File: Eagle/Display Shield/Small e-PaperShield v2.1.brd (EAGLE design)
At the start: 101.8 x 54.7 mm, 114 parts, among them J2 3300060P1-ST-TF-003A, J3 2.54-8p-male-SMD, J4 2.54-8p-male-SMD, J5 2.54-6p-male-SMD, J6 2.54-6p-male-SMD, J7 2.54-2x3p-female-SMD, Q10 MOSFET-P-044021001, Q11 2N7002, Q2 2N7002, Q3 MOSFET-P-044021001, Q5 MOSFET-P-044021001, Q7 MOSFET-P-044021001, Q8 2N7002, Q9 2N7002, SW1 BUTTON-4P-REINFORCE'TS-1188E', U2 XC6206-3.3-1300260P1, U3 74VHC125PW, U4 74VHC125PW, U5 GT20L16P1Y, U9 S-8120CNB-DRB-TF-G//200021001, X1 FH12-40S-0.5SH

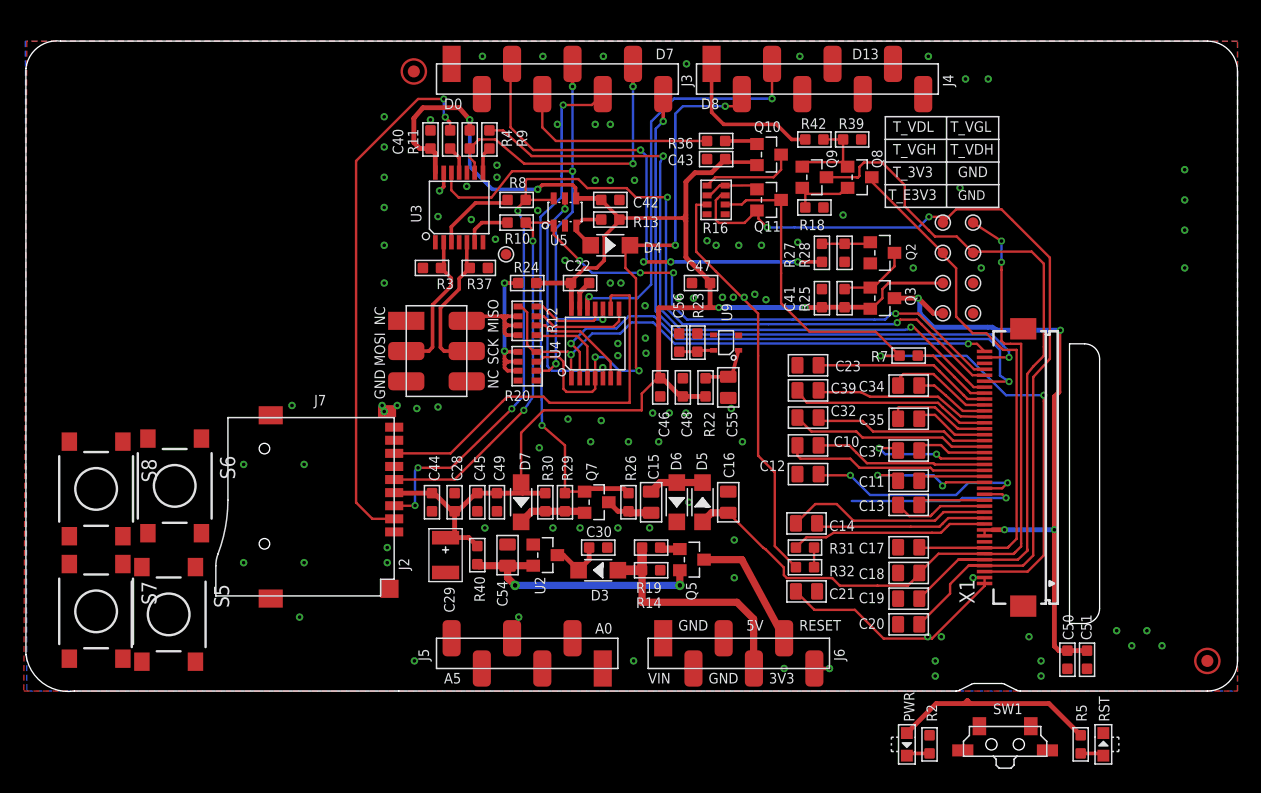
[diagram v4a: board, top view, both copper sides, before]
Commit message: DRC corrections for display shield
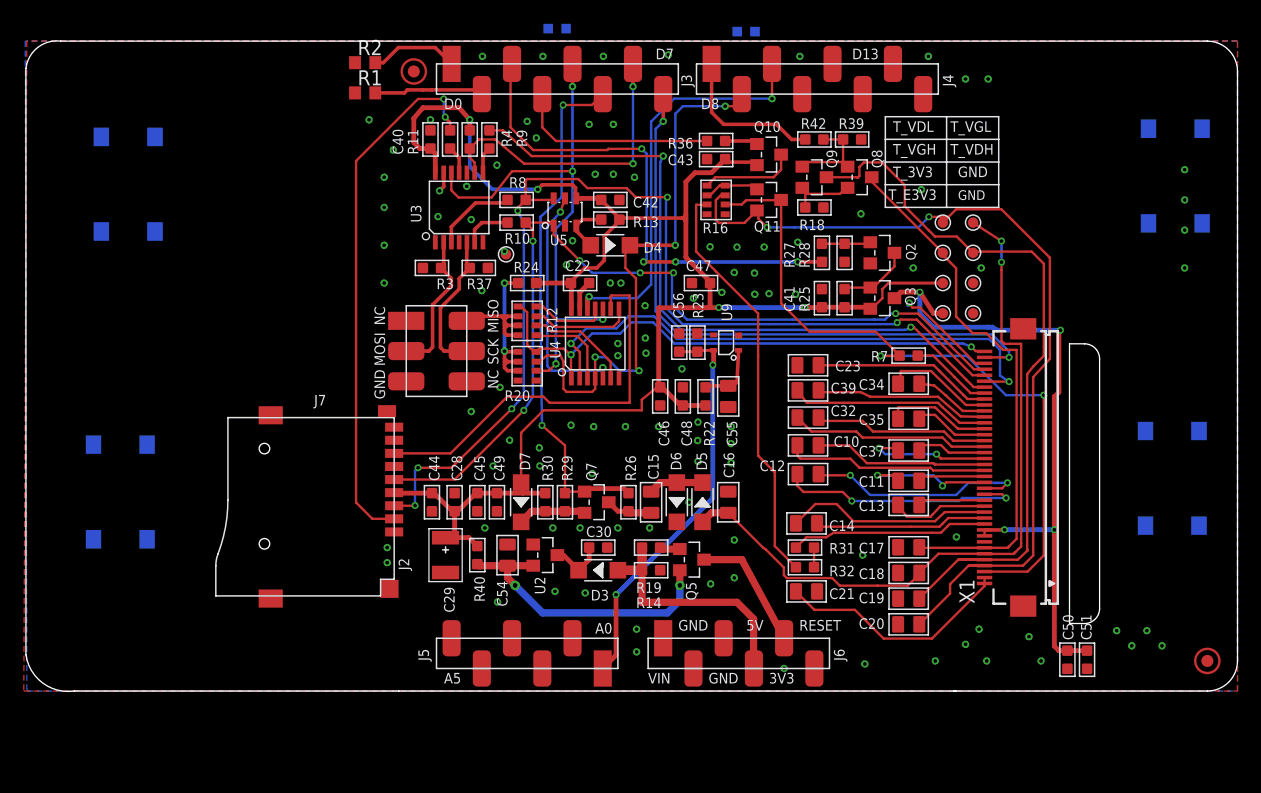
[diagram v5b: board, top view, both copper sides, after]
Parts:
- removed PWR: led-green, Discrete:LED-SIDE-VIEW-0603-RIGHT
- removed R5: 1k, Discrete:R0603
- removed RST: led-red, Discrete:LED-SIDE-VIEW-0603-RIGHT
- removed SW1: BUTTON-4P-REINFORCE'TS-1188E', Discrete:4P-SMD-7X3.5X3.5H
- added LED0: LED0, adafruit:CHIPLED_0603
- added LED1: LED1, adafruit:CHIPLED_0603
- added R1: 1k, rcl:R0603
- R2: device Discrete:R0603 -> rcl:R0603
- moved S7 97.8 mm to (96.0, 49.9), flipped to the bottom
- moved S5 85.1 mm to (95.8, 24.5), flipped to the bottom
- moved R2 74.4 mm to (27.9, 59.4), turned to 0 degrees
- moved S8 25.7 mm to (8.03, 49.2), flipped to the bottom, turned to 90 degrees
- moved S6 4.60 mm to (7.37, 23.4), flipped to the bottom
- moved C46 0.76 mm to (52.7, 31.4)
- moved C48 0.76 mm to (54.6, 31.4)
- moved C55 0.76 mm to (58.4, 31.4)
- moved R22 0.76 mm to (56.5, 31.4)
- moved C34 0.15 mm to (73.6, 32.5)
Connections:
- removed net M_CKV: J5.3
- removed net M_OE123: J5.2
- removed net M_RESET: J6.6, RST.2, SW1.2
- removed net M_STV_IN: J5.4
- removed net N$87: R5.2, RST.1
- new net BTN0: J5.2, S8.3, S8.4
- new net BTN1: J5.3, S7.3, S7.4
- new net BTN2: J5.4, S6.3, S6.4
- new net BTN3: J5.5, S5.3, S5.4
- new net LED0: J3.2, R1.2
- new net LED1: J3.1, R2.2
- new net N$17: LED1.A, R2.1
- net GND: now also LED0.C, LED1.C, S5.1, S5.2, S6.1, S6.2, S7.1, S7.2, S8.1, S8.2; no longer R2.2, SW1.1, SW1.S1, SW1.S2
- net N$1: now also LED0.A, R1.1; no longer PWR.2, R2.1
- net VCC_3V3: no longer PWR.1, R5.1
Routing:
- net M_TEMP_SEN: track 2.92 -> 33.5 mm, vias 0 -> 2
- net VCC_3V3: track 161.9 -> 144.3 mm
- net LED0: track 0.00 -> 9.21 mm
- net GND: track 4.16 -> 12.9 mm, vias 105 -> 106
- net LED1: track 0.00 -> 7.51 mm
- net N$97: track 15.0 -> 21.1 mm, vias 1 -> 2
- net VCC_OUT: track 21.8 -> 24.4 mm
- net N$1: track 1.99 -> 0.00 mm
- net N$87: track 1.98 -> 0.00 mm
- net M_RESET: track 1.27 -> 0.00 mm, vias 1 -> 0
- net VCC_3V3_EPD: track 56.0 -> 57.1 mm
- net VDD: track 4.81 -> 5.45 mm
- net N$34: track 9.21 -> 9.78 mm
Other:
- outline, holes or cut-outs redrawn
- board text added: "/Users/raffael/Desktop/EPFL Master/CHIC/dOry_logo_mono.bmp"
- board text added: "edited by dOry"
- board text added: "version dOry 22/05/2015"
- board text removed: "v2.1 11/05/2013"

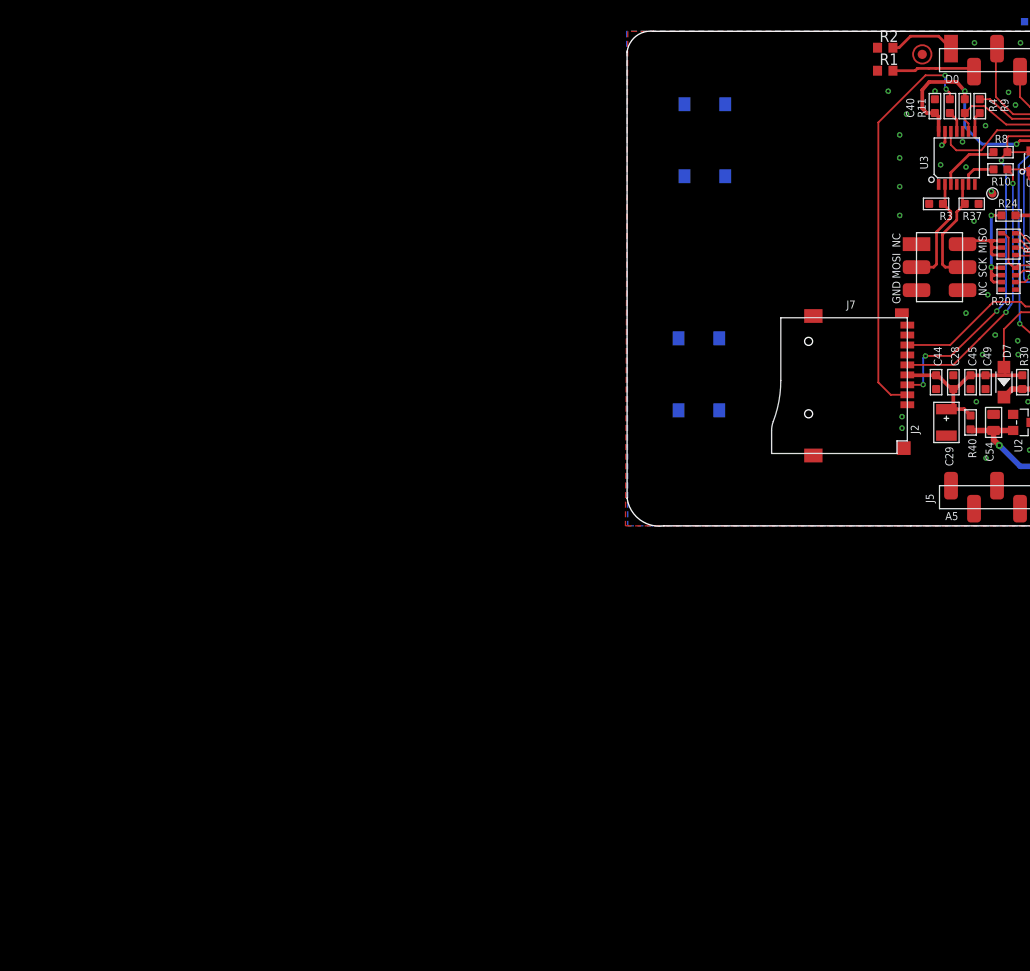
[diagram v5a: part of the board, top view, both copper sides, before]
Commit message: added pull-ups for buttons on display shield
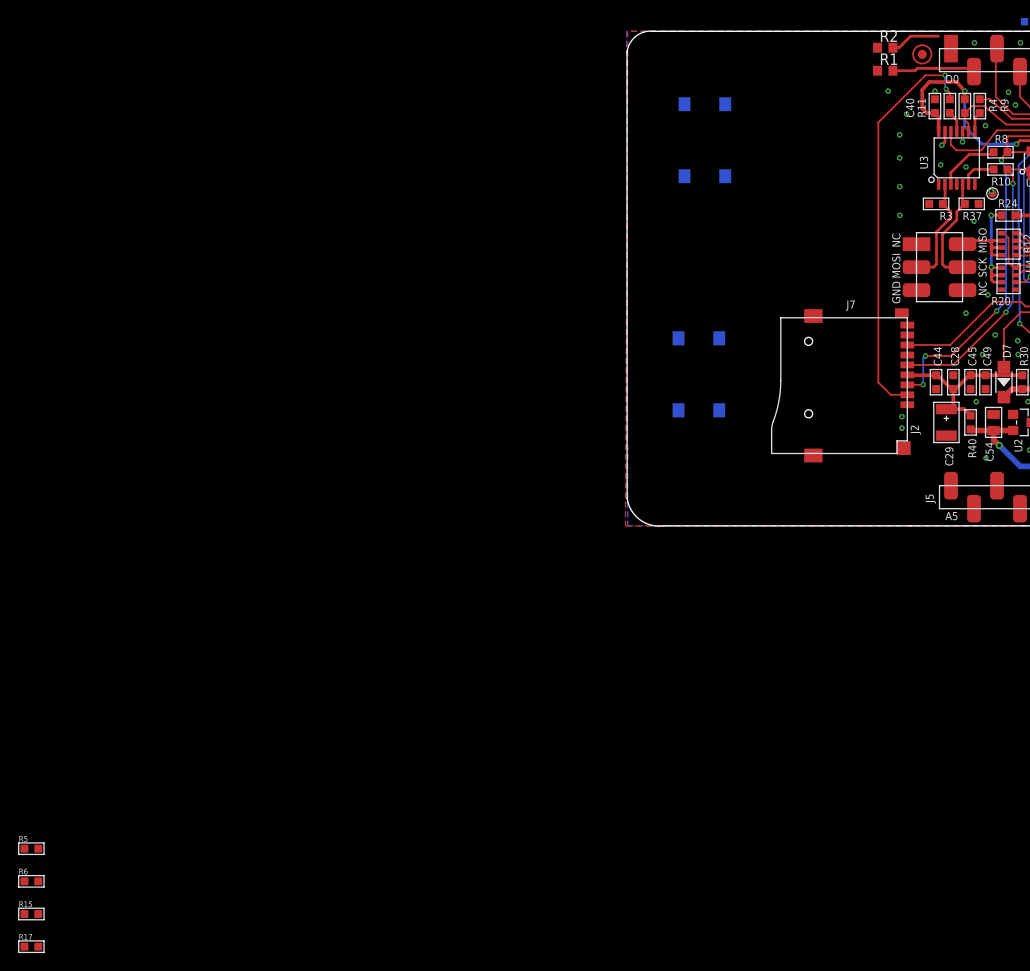
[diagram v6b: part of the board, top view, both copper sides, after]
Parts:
- added R15, R17, R5, R6: 10k, Discrete:R0603
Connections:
- net BTN0: now also R5.2
- net BTN1: now also R6.2
- net BTN2: now also R15.2
- net BTN3: now also R17.2
- net LED0: now also J3.1; no longer J3.2
- net LED1: now also J3.2; no longer J3.1
- net M_VCC_3V3: now also R15.1, R17.1, R5.1, R6.1
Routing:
- net LED1: track 7.51 -> 5.57 mm
- net LED0: track 9.21 -> 8.70 mm
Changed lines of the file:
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@@
 <element name="LED1" library="adafruit" package="CHIPLED_0603" value="LED1" x="59.949" y="62.049" rot="MR90"/>
 <element name="R2" library="rcl" package="R0603" value="1k" x="27.94" y="59.436"/>
+<element name="R5" library="Discrete" package="R0603" value="10k" x="-66.3448" y="-29.0068"/>
+<element name="R6" library="Discrete" package="R0603" value="10k" x="-66.3448" y="-32.6136"/>
+<element name="R15" library="Discrete" package="R0603" value="10k" x="-66.3448" y="-36.2204"/>
+<element name="R17" library="Discrete" package="R0603" value="10k" x="-66.3448" y="-39.8272"/>
 </elements>
 <signals>
@@
 <wire x1="63.1444" y1="11.0744" x2="59.5884" y2="17.6784" width="0.6096" layer="1"/>
 <wire x1="59.5884" y1="17.6784" x2="56.4134" y2="17.6784" width="0.6096" layer="1"/>
+<contactref element="R5" pad="1"/>
+<contactref element="R6" pad="1"/>
+<contactref element="R15" pad="1"/>
+<contactref element="R17" pad="1"/>
+<wire x1="-67.1068" y1="-36.2204" x2="-67.1068" y2="-39.8272" width="0" layer="19" extent="1-1"/>
+<wire x1="-67.1068" y1="-32.6136" x2="-67.1068" y2="-36.2204" width="0" layer="19" extent="1-1"/>
+<wire x1="-67.1068" y1="-29.0068" x2="-67.1068" y2="-32.6136" width="0" layer="19" extent="1-1"/>
+<wire x1="56.4134" y1="17.6784" x2="-67.1068" y2="-29.0068" width="0" layer="19" extent="1-1"/>
 </signal>
 <signal name="M_VCC_5V">
@@
 </signal>
 <signal name="LED1">
-<contactref element="J3" pad="1"/>
 <contactref element="R2" pad="2"/>
-<wire x1="35.2044" y1="59.3344" x2="33.8328" y2="60.706" width="0.3048" layer="1"/>
 <wire x1="33.8328" y1="60.706" x2="30.734" y2="60.706" width="0.3048" layer="1"/>
 <wire x1="30.734" y1="60.706" x2="29.464" y2="59.436" width="0.3048" layer="1"/>
 <wire x1="29.464" y1="59.436" x2="28.79" y2="59.436" width="0.3048" layer="1"/>
+<contactref element="J3" pad="2"/>
+<wire x1="33.8328" y1="60.706" x2="37.7444" y2="56.7944" width="0" layer="19" extent="1-1"/>
 </signal>
 <signal name="LED0">
-<contactref element="J3" pad="2"/>
 <contactref element="R1" pad="2"/>
-<wire x1="37.7444" y1="56.7944" x2="37.3888" y2="57.15" width="0.3048" layer="1"/>
 <wire x1="37.3888" y1="57.15" x2="33.528" y2="57.15" width="0.3048" layer="1"/>
 <wire x1="33.528" y1="57.15" x2="32.766" y2="57.15" width="0.3048" layer="1"/>
@@
 <wire x1="31.496" y1="57.15" x2="31.242" y2="56.896" width="0.3048" layer="1"/>
 <wire x1="31.242" y1="56.896" x2="28.79" y2="56.896" width="0.3048" layer="1"/>
+<contactref element="J3" pad="1"/>
+<wire x1="33.528" y1="57.15" x2="35.2044" y2="59.3344" width="0" layer="19" extent="1-1"/>
 </signal>
 <signal name="BTN3">
@@
 <contactref element="J5" pad="5"/>
 <contactref element="S5" pad="4"/>
+<contactref element="R17" pad="2"/>
 <wire x1="98.008" y1="20.536" x2="98.008" y2="28.486" width="0" layer="19" extent="16-16"/>
 <wire x1="37.7444" y1="8.5344" x2="98.008" y2="20.536" width="0" layer="19" extent="1-16"/>
+<wire x1="-65.5828" y1="-39.8272" x2="37.7444" y2="8.5344" width="0" layer="19" extent="1-1"/>
 </signal>
 <signal name="BTN2">
@@
 <contactref element="J5" pad="4"/>
 <contactref element="S6" pad="4"/>
-<wire x1="9.616" y1="19.393" x2="40.2844" y2="11.0744" width="0" layer="19" extent="1-16"/>
+<contactref element="R15" pad="2"/>
+<wire x1="9.616" y1="19.393" x2="-65.5828" y2="-36.2204" width="0" layer="19" extent="1-16"/>
 <wire x1="9.616" y1="27.343" x2="9.616" y2="19.393" width="0" layer="19" extent="16-16"/>
+<wire x1="40.2844" y1="11.0744" x2="9.616" y2="19.393" width="0" layer="19" extent="1-16"/>
 </signal>
 <signal name="BTN1">
@@
 <contactref element="J5" pad="3"/>
 <contactref element="S7" pad="4"/>
+<contactref element="R6" pad="2"/>
 <wire x1="98.262" y1="45.936" x2="98.262" y2="53.886" width="0" layer="19" extent="16-16"/>
 <wire x1="42.8244" y1="8.5344" x2="98.262" y2="45.936" width="0" layer="19" extent="1-16"/>
+<wire x1="-65.5828" y1="-32.6136" x2="42.8244" y2="8.5344" width="0" layer="19" extent="1-1"/>
 </signal>
 <signal name="BTN0">
@@
 <contactref element="J5" pad="2"/>
 <contactref element="S8" pad="4"/>
-<wire x1="5.7764" y1="45.2502" x2="5.7764" y2="53.2002" width="0" layer="19" extent="16-16"/>
+<contactref element="R5" pad="2"/>
+<wire x1="5.7764" y1="45.2502" x2="-65.5828" y2="-29.0068" width="0" layer="19" extent="1-16"/>
+<wire x1="5.7764" y1="53.2002" x2="5.7764" y2="45.2502" width="0" layer="19" extent="16-16"/>
 <wire x1="45.3644" y1="11.0744" x2="5.7764" y2="45.2502" width="0" layer="19" extent="1-16"/>
 </signal>

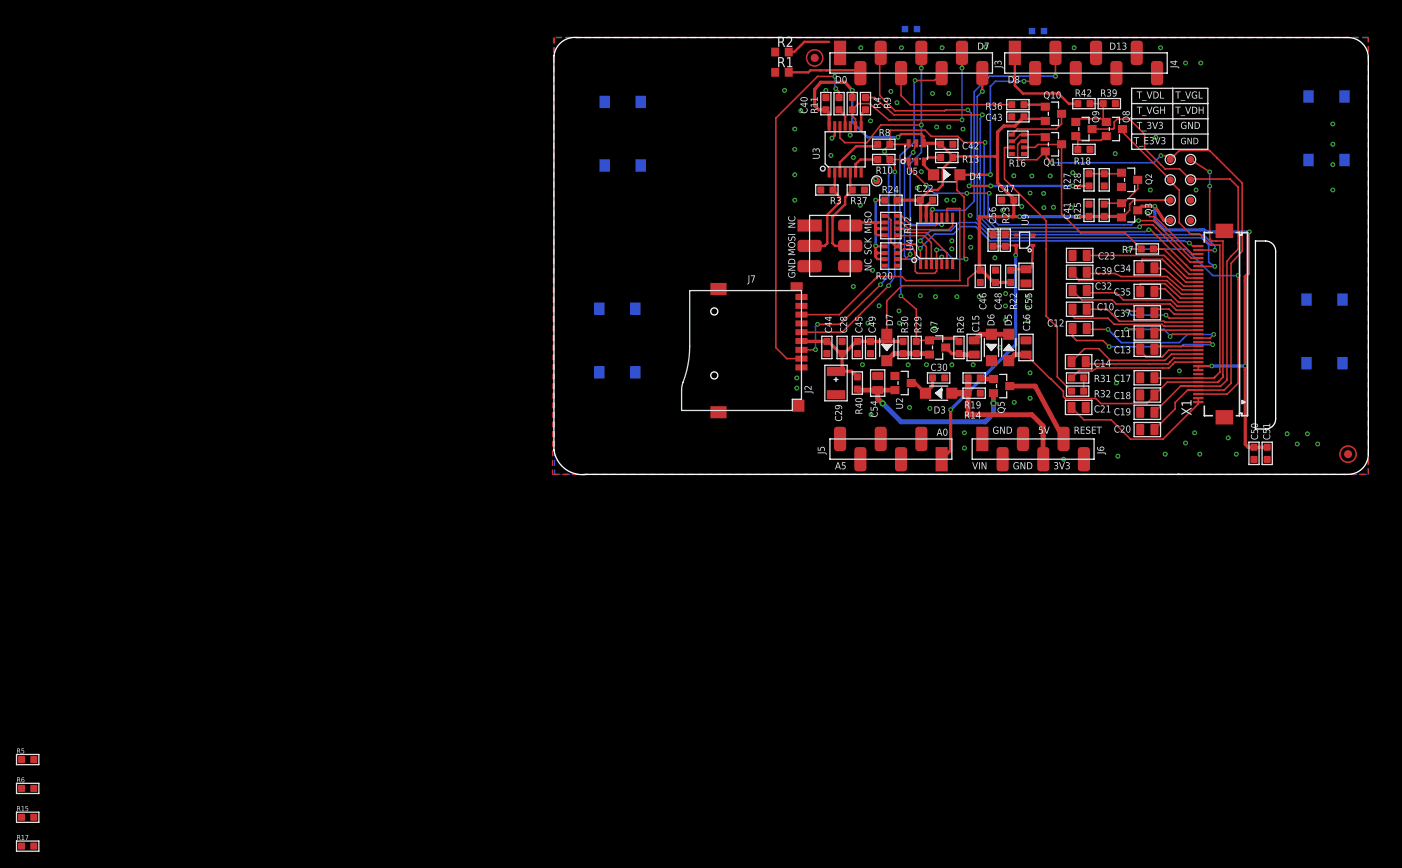
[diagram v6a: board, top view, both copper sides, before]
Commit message: resized display shield, placed buttons and leds to their final position
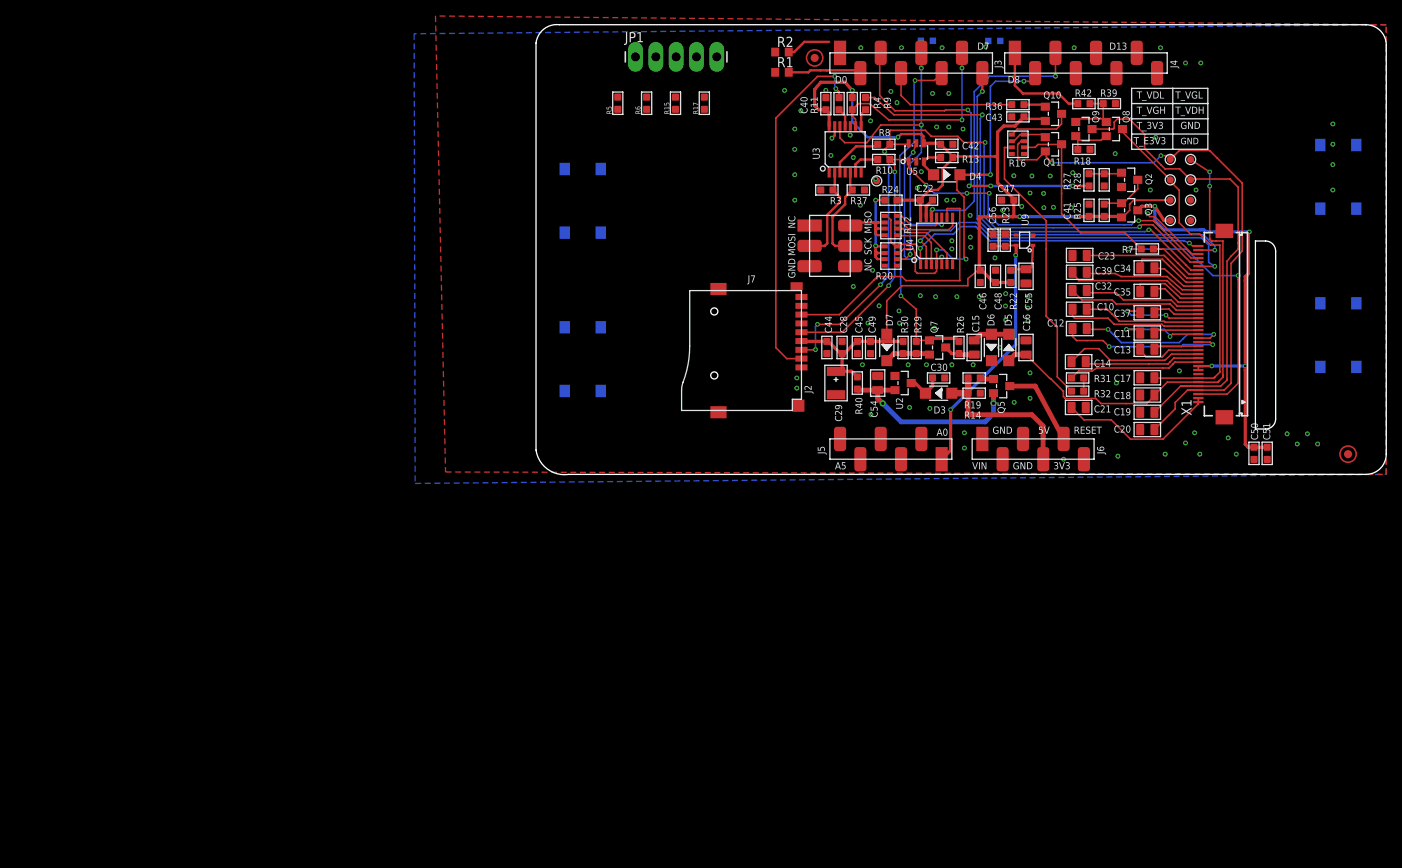
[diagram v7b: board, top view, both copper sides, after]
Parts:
- added JP1: (no value), SparkFun-Connectors:1X05_LONGPADS
- moved R17 125.6 mm to (18.2, 53.0), turned to 90 degrees
- moved R15 120.5 mm to (14.6, 53.0), turned to 90 degrees
- moved R6 115.4 mm to (11.0, 53.0), turned to 90 degrees
- moved R5 110.3 mm to (7.42, 53.0), turned to 90 degrees
- moved S8 9.76 mm to (3.05, 40.8)
- moved S7 6.26 mm to (97.5, 43.8)
- moved LED1 5.60 mm to (54.5, 60.8)
- moved S6 4.90 mm to (3.05, 21.0)
- moved LED0 2.47 mm to (46.1, 60.8)
- moved S5 1.79 mm to (97.5, 24.1)
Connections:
- net BTN0: now also JP1.1
- net BTN1: now also JP1.2
- net BTN2: now also JP1.3
- net BTN3: now also JP1.4
- net GND: now also JP1.5
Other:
- board size 101.8 x 54.7 mm -> 106.3 x 56.3 mm
